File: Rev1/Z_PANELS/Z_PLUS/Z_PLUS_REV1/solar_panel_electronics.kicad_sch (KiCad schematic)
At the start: 22 parts, among them IC2 SM141K04TFV, IC3 SM141K04TFV, IC4 SM141K04TFV, IC5 SM141K04TFV, U2 LTC3130EUDC-1-PBF

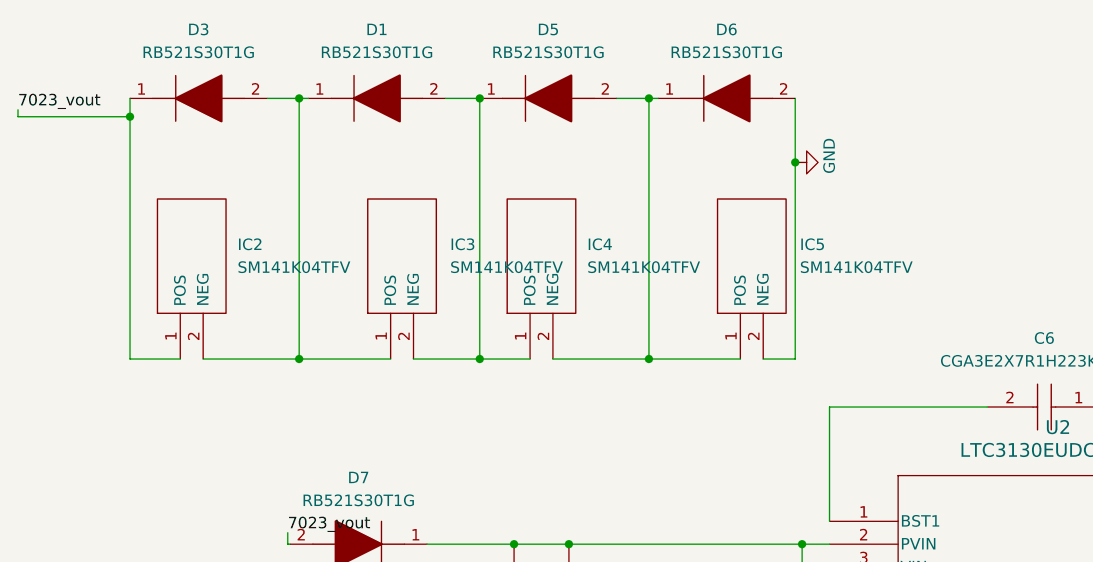
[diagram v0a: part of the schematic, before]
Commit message: finished Z minus board design
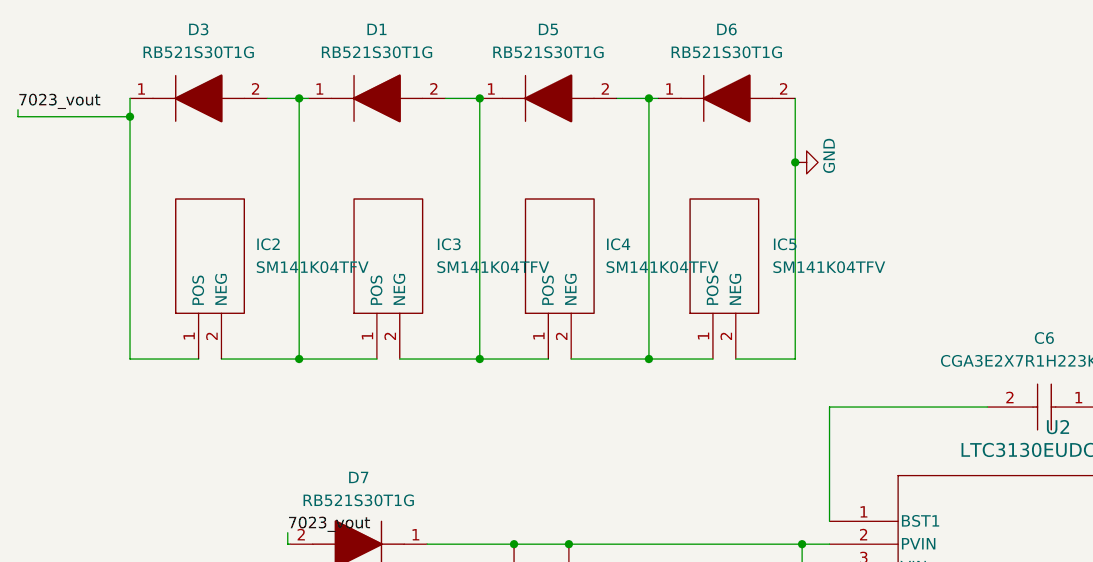
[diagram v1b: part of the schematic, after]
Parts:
- IC2, IC3, IC4, IC5: footprint SODFL490150X120N -> SODFL340230X120N
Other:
- moved on the sheet: IC2, IC3, IC4, IC5

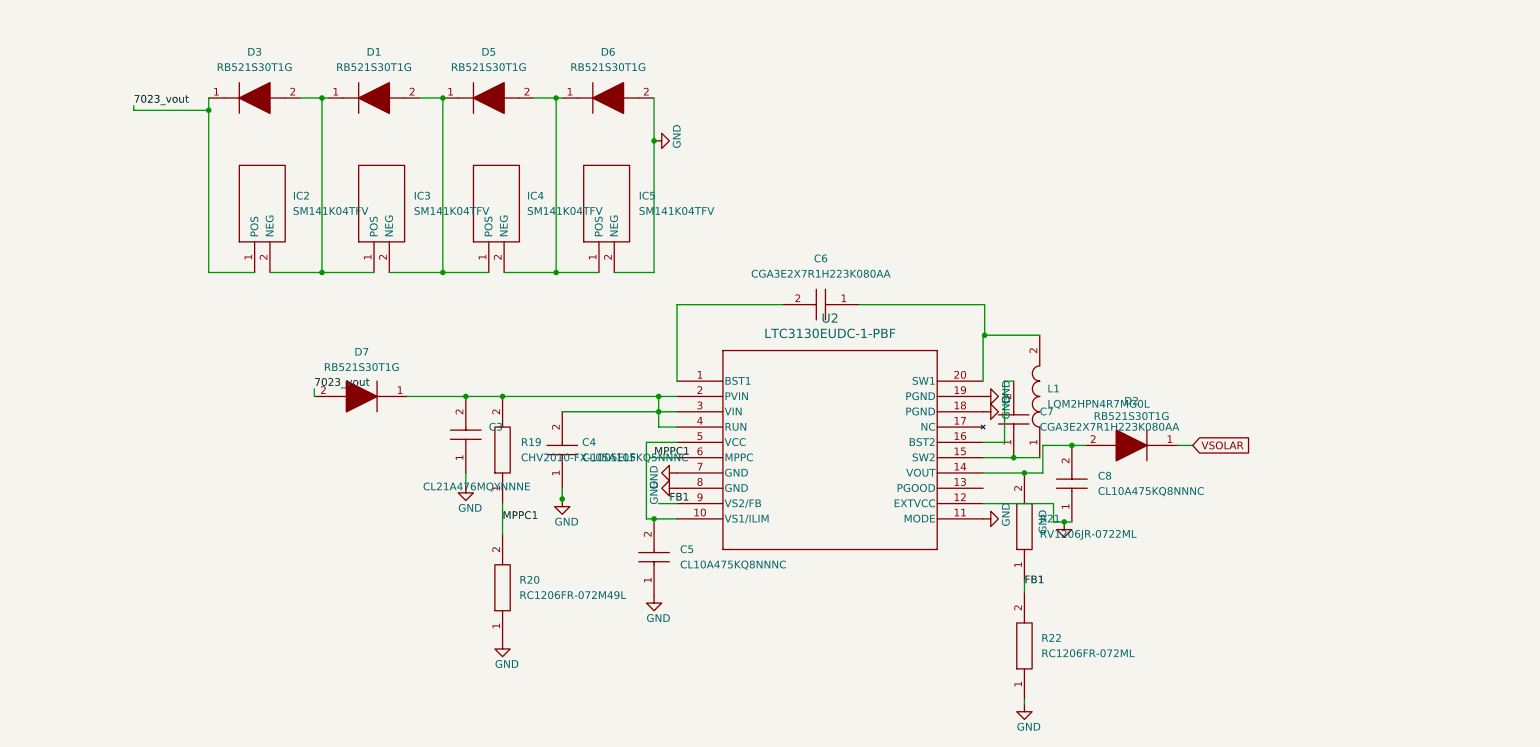
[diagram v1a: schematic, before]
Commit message: fixed bug in Z minus
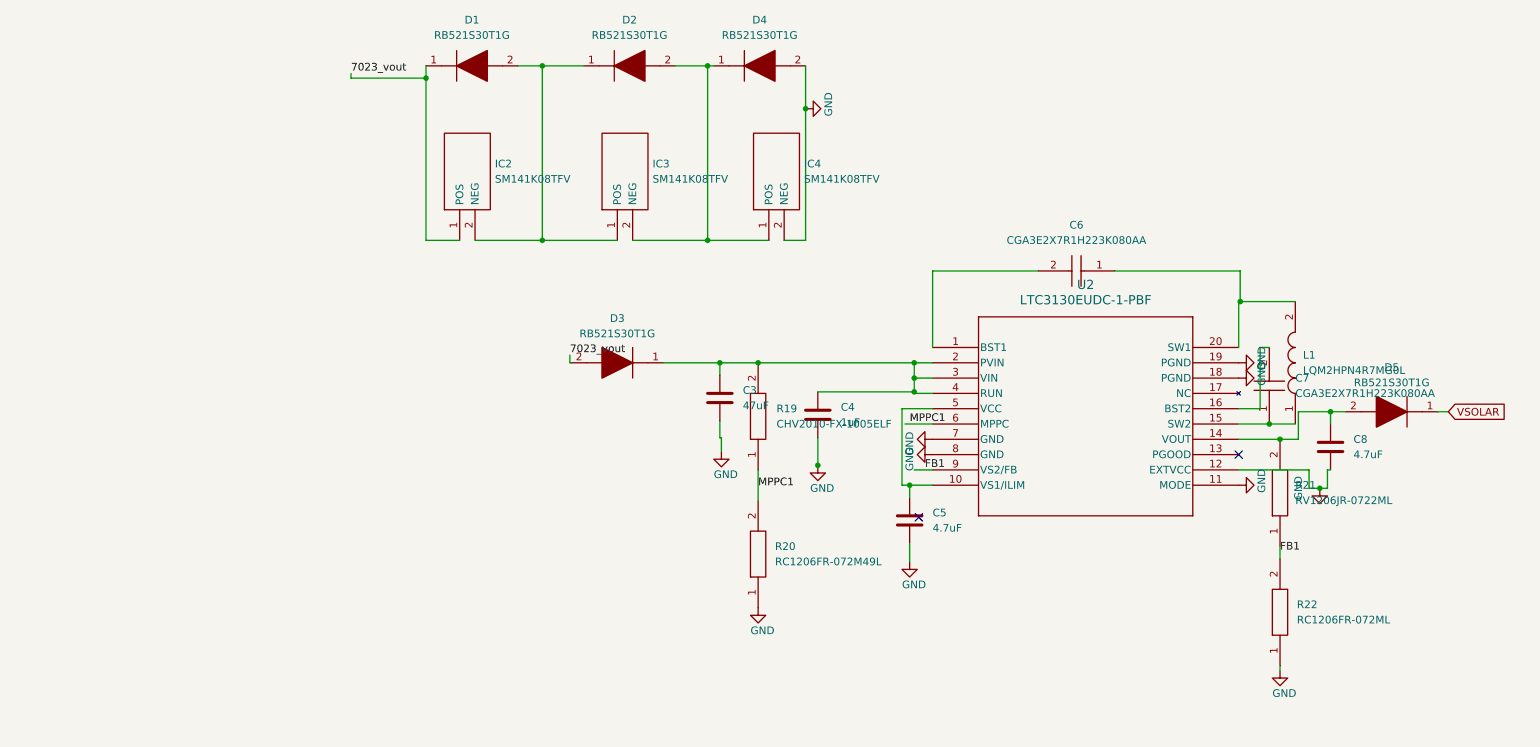
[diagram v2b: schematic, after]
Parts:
- removed C3: CL21A476MQYNNNE, CAPC2012X135N, symbol AA_AUTO_LOADER:CL21A476MQYNNNE
- removed C4: CL05A105KQ5NNNC, CAPC1005X55N, symbol AA_AUTO_LOADER:CL05A105KQ5NNNC
- removed C5, C8: CL10A475KQ8NNNC, CAPC1608X90N, symbol AA_AUTO_LOADER:CL10A475KQ8NNNC
- removed D6, D7: RB521S30T1G, SODFL1608X70N, symbol AA_AUTO_LOADER:RB521S30T1G
- removed IC2, IC3, IC4, IC5: SM141K04TFV, SODFL340230X120N, symbol AA_AUTO_LOADER:SM141K04TFV
- added C3: 47uF, Capacitor_SMD:C_0805_2012Metric, symbol PCM_Capacitor_AKL:C_0805
- added C4: 1uF, Capacitor_SMD:C_0805_2012Metric, symbol PCM_Capacitor_AKL:C_0805
- added C5, C8: 4.7uF, Capacitor_SMD:C_0805_2012Metric, symbol PCM_Capacitor_AKL:C_0805
- added D4: RB521S30T1G, SODFL1608X70N, symbol AA_AUTO_LOADER:RB521S30T1G
- added IC2, IC3, IC4: SM141K08TFV, SODFL520290X120N, symbol AA_AUTO_LOADER:SM141K08TFV
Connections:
- net 7023_vout: now also D1.1, D3.2, IC2.1 (POS); no longer D3.1
- net GND: now also C3.2, C4.2, C5.2, C8.2, D4.2, IC4.2 (NEG)
- net VSOLAR: now also D5.1; no longer D2.1
- net at D1.2: now also D2.1, IC2.2 (NEG), IC3.1 (POS); no longer D5.1
- net at D5.2: now also R21.2, U2.14 (VOUT), C8.1
- net at U2.10 (VS1/ILIM), U2.5 (VCC): now also C5.1
- net at R19.2, U2.2 (PVIN), U2.3 (VIN)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: now also D3.1, C3.1, C4.1
- new net: D2.2, D4.1, IC3.2 (NEG), IC4.1 (POS)
- no-connect marks 0 -> 2

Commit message: CHANGED Resistor values for MPPC; added testpoints and silkscreen info
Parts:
- R19: value CHV2010-FX-1005ELF -> 12M
- R20: value RC1206FR-072M49L -> 1M
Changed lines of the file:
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@@
       (effects (font (size 1.27 1.27)) (justify right))
     )
-    (property "Value" "RC1206FR-072M49L" (at 154.178 117.348 90)
+    (property "Value" "1M" (at 154.178 117.348 90)
       (effects (font (size 1.27 1.27)) (justify right))
     )
@@
       (effects (font (size 1.27 1.27)) (justify right))
     )
-    (property "Value" "CHV2010-FX-1005ELF" (at 154.432 94.488 90)
-      (effects (font (size 1.27 1.27)) (justify right))
-    )
+    (property "Value" "12M" (at 154.432 94.488 90)
+      (effects (font (size 1.27 1.27)) (justify right))
+    )

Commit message: made diode changes and schematic changes
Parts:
- removed D1, D2, D3, D4, D5: RB521S30T1G, SODFL1608X70N, symbol AA_AUTO_LOADER:RB521S30T1G
- removed R21: RV1206JR-0722ML, RESC3116X65N, symbol AA_AUTO_LOADER:RV1206JR-0722ML
- removed R22: RC1206FR-072ML, RESC3116X65N, symbol AA_AUTO_LOADER:RC1206FR-072ML
- added D1, D2, D3, D4, D5: LSM115JE3_TR13, DIOM5436X330N, symbol AA_AUTO_LOADER:LSM115JE3_TR13
- renumbered C8 to C10, C3 to C5, C4 to C6, C5 to C7, C6 to C8, C7 to C9, IC4 to IC2, IC2 to IC4
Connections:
- net FB1 is gone; now on an unnamed net: U2.9 (VS2/FB)
- net 7023_vout: now also D3.1, D4.2
- net GND: now also U2.17 (NC), D1.2
- net VSOLAR: now also D5.1
- net at C10.1, U2.14 (VOUT): now also D5.2
- net at IC3.1 (POS), IC4.2 (NEG): now also D2.1, D3.2
- net at IC2.1 (POS), IC3.2 (NEG): now also D1.1, D2.2
- net at C5.1, C6.1, R19.2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: now also D4.1
- no-connect marks 2 -> 1
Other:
- moved on the sheet: IC2, IC3, IC4

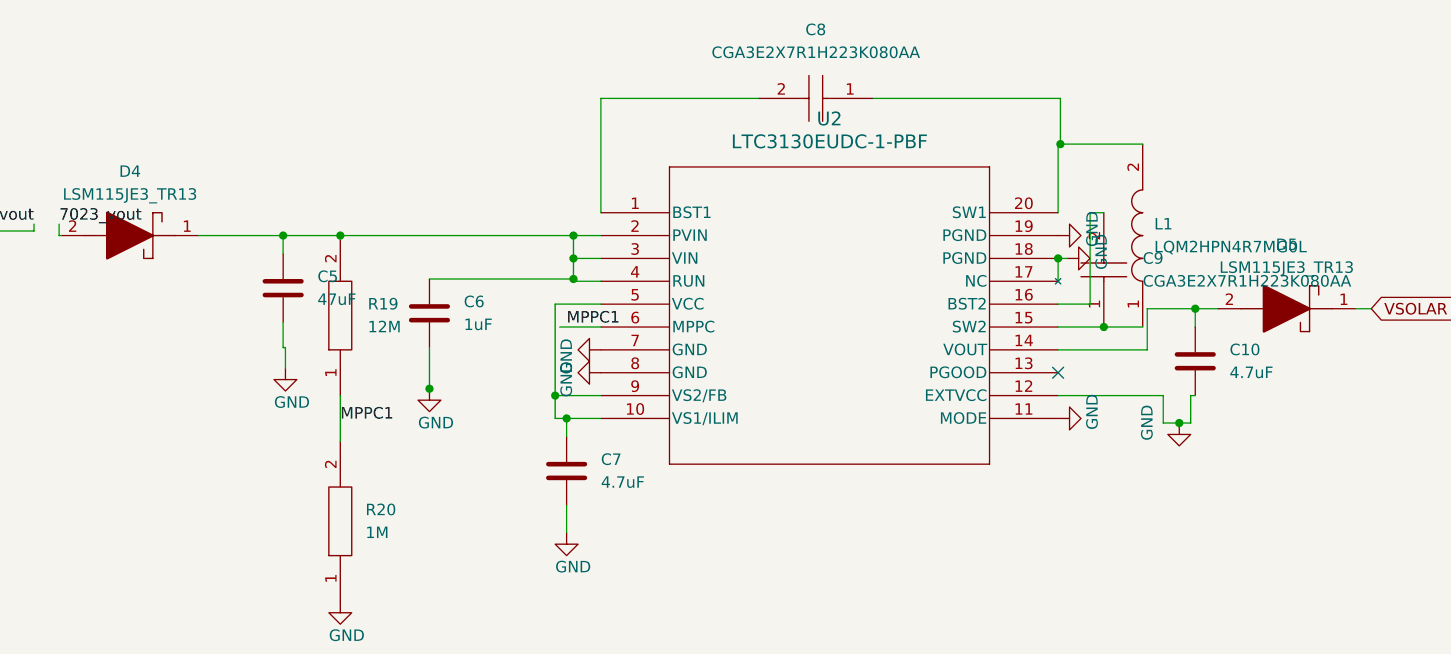
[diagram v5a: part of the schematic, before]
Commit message: updated ltc3130 schematic
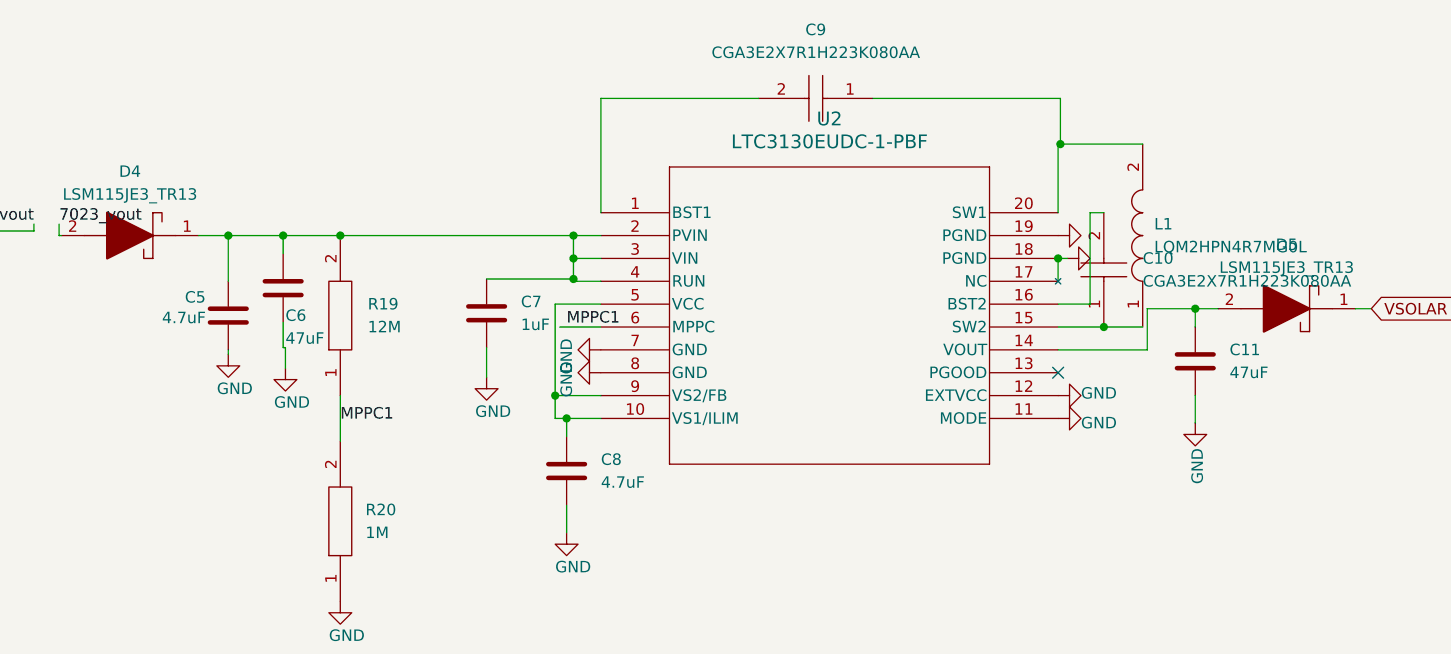
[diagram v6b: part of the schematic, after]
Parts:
- added C5: 4.7uF, Capacitor_SMD:C_0805_2012Metric, symbol PCM_Capacitor_AKL:C_0805
- C11: renamed from C10; value 4.7uF -> 47uF
- renumbered C9 to C10, C5 to C6, C6 to C7, C7 to C8, C8 to C9
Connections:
- net GND: now also C5.2
- net at C6.1, C7.1, D4.1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: now also C5.1
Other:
- moved on the sheet: C7

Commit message: Z PLUS Updated
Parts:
- added TP1, TP2: TestPoint, TestPoint:TestPoint_Loop_D1.80mm_Drill1.0mm_Beaded, symbol Connector:TestPoint
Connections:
- net GND: now also U2.21 (PAD), TP2.1
- net VSOLAR: now also TP1.1
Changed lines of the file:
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@@
 (kicad_sch (version 20230121) (generator eeschema)
   (paper "A4")
+  (junction (at 175.26 102.108) (diameter 0) (color 0 0 0 0)
+  )
+  (junction (at 222.758 117.348) (diameter 0) (color 0 0 0 0)
+  )
+  (junction (at 58.166 110.744) (diameter 0) (color 0 0 0 0)
+  )
+  (junction (at 58.166 81.788) (diameter 0) (color 0 0 0 0)
+  )
+  (junction (at 176.53 104.648) (diameter 0) (color 0 0 0 0)
+  )
+  (junction (at 265.684 92.456) (diameter 0) (color 0 0 0 0)
+  )
+  (junction (at 138.938 84.328) (diameter 0) (color 0 0 0 0)
+  )
+  (junction (at 236.22 94.488) (diameter 0) (color 0 0 0 0)
+  )
+  (junction (at 41.91 88.9) (diameter 0) (color 0 0 0 0)
+  )
+  (junction (at 104.902 83.82) (diameter 0) (color 0 0 0 0)
+  )
   (junction (at 231.14 86.868) (diameter 0) (color 0 0 0 0)
   )
-  (junction (at 175.26 102.108) (diameter 0) (color 0 0 0 0)
-  )
-  (junction (at 58.166 110.744) (diameter 0) (color 0 0 0 0)
-  )
-  (junction (at 58.166 81.788) (diameter 0) (color 0 0 0 0)
-  )
-  (junction (at 176.53 104.648) (diameter 0) (color 0 0 0 0)
-  )
-  (junction (at 138.938 84.328) (diameter 0) (color 0 0 0 0)
-  )
-  (junction (at 236.22 94.488) (diameter 0) (color 0 0 0 0)
-  )
-  (junction (at 41.91 88.9) (diameter 0) (color 0 0 0 0)
-  )
-  (junction (at 104.902 83.82) (diameter 0) (color 0 0 0 0)
-  )
   (junction (at 151.384 84.328) (diameter 0) (color 0 0 0 0)
   )
@@
   )
   (junction (at 85.598 110.744) (diameter 0) (color 0 0 0 0)
+  )
+  (junction (at 231.14 104.648) (diameter 0) (color 0 0 0 0)
   )
   (junction (at 177.292 86.868) (diameter 0) (color 0 0 0 0)
@@
     (stroke (width 0) (type default))
   )
+  (wire (pts (xy 204.47 117.348) (xy 222.758 117.348))
+    (stroke (width 0) (type default))
+  )
   (wire (pts (xy 85.598 81.788) (xy 85.598 110.744))
     (stroke (width 0) (type default))
@@
     (stroke (width 0) (type default))
   )
+  (wire (pts (xy 265.684 92.456) (xy 265.938 92.456))
+    (stroke (width 0) (type default))
+  )
   (wire (pts (xy 138.938 97.536) (xy 138.938 97.028))
     (stroke (width 0) (type default))
@@
     (stroke (width 0) (type default))
   )
+  (wire (pts (xy 231.14 86.868) (xy 231.14 89.408))
+    (stroke (width 0) (type default))
+  )
   (wire (pts (xy 177.292 89.154) (xy 177.292 89.408))
     (stroke (width 0) (type default))
@@
     (stroke (width 0) (type default))
   )
-  (wire (pts (xy 264.16 92.456) (xy 265.938 92.456))
+  (wire (pts (xy 264.16 92.456) (xy 265.684 92.456))
     (stroke (width 0) (type default))
   )
@@
     (stroke (width 0) (type default))
   )
+  (wire (pts (xy 231.14 104.648) (xy 231.14 117.348))
+    (stroke (width 0) (type default))
+  )
   (wire (pts (xy 41.91 88.9) (xy 41.91 110.744))
     (stroke (width 0) (type default))
@@
     (stroke (width 0) (type default))
   )
-  (wire (pts (xy 231.14 89.408) (xy 231.14 86.868))
-    (stroke (width 0) (type default))
-  )
   (wire (pts (xy 58.166 81.788) (xy 58.166 110.744))
     (stroke (width 0) (type default))
@@
   )
   (wire (pts (xy 176.53 106.68) (xy 176.53 104.648))
+    (stroke (width 0) (type default))
+  )
+  (wire (pts (xy 222.758 117.348) (xy 231.14 117.348))
     (stroke (width 0) (type default))
   )
@@
         (path "/97119169-578f-44be-8822-faf8f0e4fcd6/db306d3f-1ab7-4e38-afab-c78bdb56c587"
           (reference "#PWR042") (unit 1)
+        )
+      )
+    )
+  )
+  (symbol (lib_id "Connector:TestPoint") (at 222.758 117.348 0) (unit 1)
+    (in_bom yes) (on_board yes) (dnp no) (fields_autoplaced)
+    (property "Reference" "TP2" (at 225.044 112.776 0)
+      (effects (font (size 1.27 1.27)) (justify left))
+    )
+    (property "Value" "TestPoint" (at 225.044 115.316 0)
+      (effects (font (size 1.27 1.27)) (justify left))
+    )
+    (property "Footprint" "TestPoint:TestPoint_Loop_D1.80mm_Drill1.0mm_Beaded" (at 227.838 117.348 0)
+      (effects (font (size 1.27 1.27)) hide)
+    )
+    (property "Datasheet" "~" (at 227.838 117.348 0)
+      (effects (font (size 1.27 1.27)) hide)
+    )
+    (pin "1")
+    (instances
+      (project "Z_PLUS_REV1"
+        (path "/39cf28b0-d395-4333-bc0e-a98538893595/b8717c54-ec37-498b-9d48-acf0e788946a"
+          (reference "TP2") (unit 1)
         )
       )
@@
     (pin "15")
     (pin "16")
-    (pin "17")
     (pin "18")
     (pin "19")
@@
     (pin "8")
     (pin "9")
+    (pin "17")
+    (pin "21")
     (instances
       (project "Z_PLUS_REV1"
@@
         )
       )
+    )
+  )
+  (symbol (lib_id "Connector:TestPoint") (at 265.684 92.456 0) (unit 1)
+    (in_bom yes) (on_board yes) (dnp no) (fields_autoplaced)
+    (property "Reference" "TP1" (at 267.97 87.884 0)
+      (effects (font (size 1.27 1.27)) (justify left))
+    )
+    (property "Value" "TestPoint" (at 267.97 90.424 0)
+      (effects (font (size 1.27 1.27)) (justify left))
+    )
+    (property "Footprint" "TestPoint:TestPoint_Loop_D1.80mm_Drill1.0mm_Beaded" (at 270.764 92.456 0)
+      (effects (font (size 1.27 1.27)) hide)
+    )
+    (property "Datasheet" "~" (at 270.764 92.456 0)
+      (effects (font (size 1.27 1.27)) hide)
+    )
+    (pin "1")
+    (instances
+      (project "Z_PLUS_REV1"
+        (path "/39cf28b0-d395-4333-bc0e-a98538893595/b8717c54-ec37-498b-9d48-acf0e788946a"
+          (reference "TP1") (unit 1)
+        )
+      )
